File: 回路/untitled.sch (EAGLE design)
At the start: 213 parts, among them Q1 2SJ626, Q2 2SJ626, Q3 BSS138, Q4 BSS138, Q5 2SJ626, Q6 BSS138, Q7 BSS138

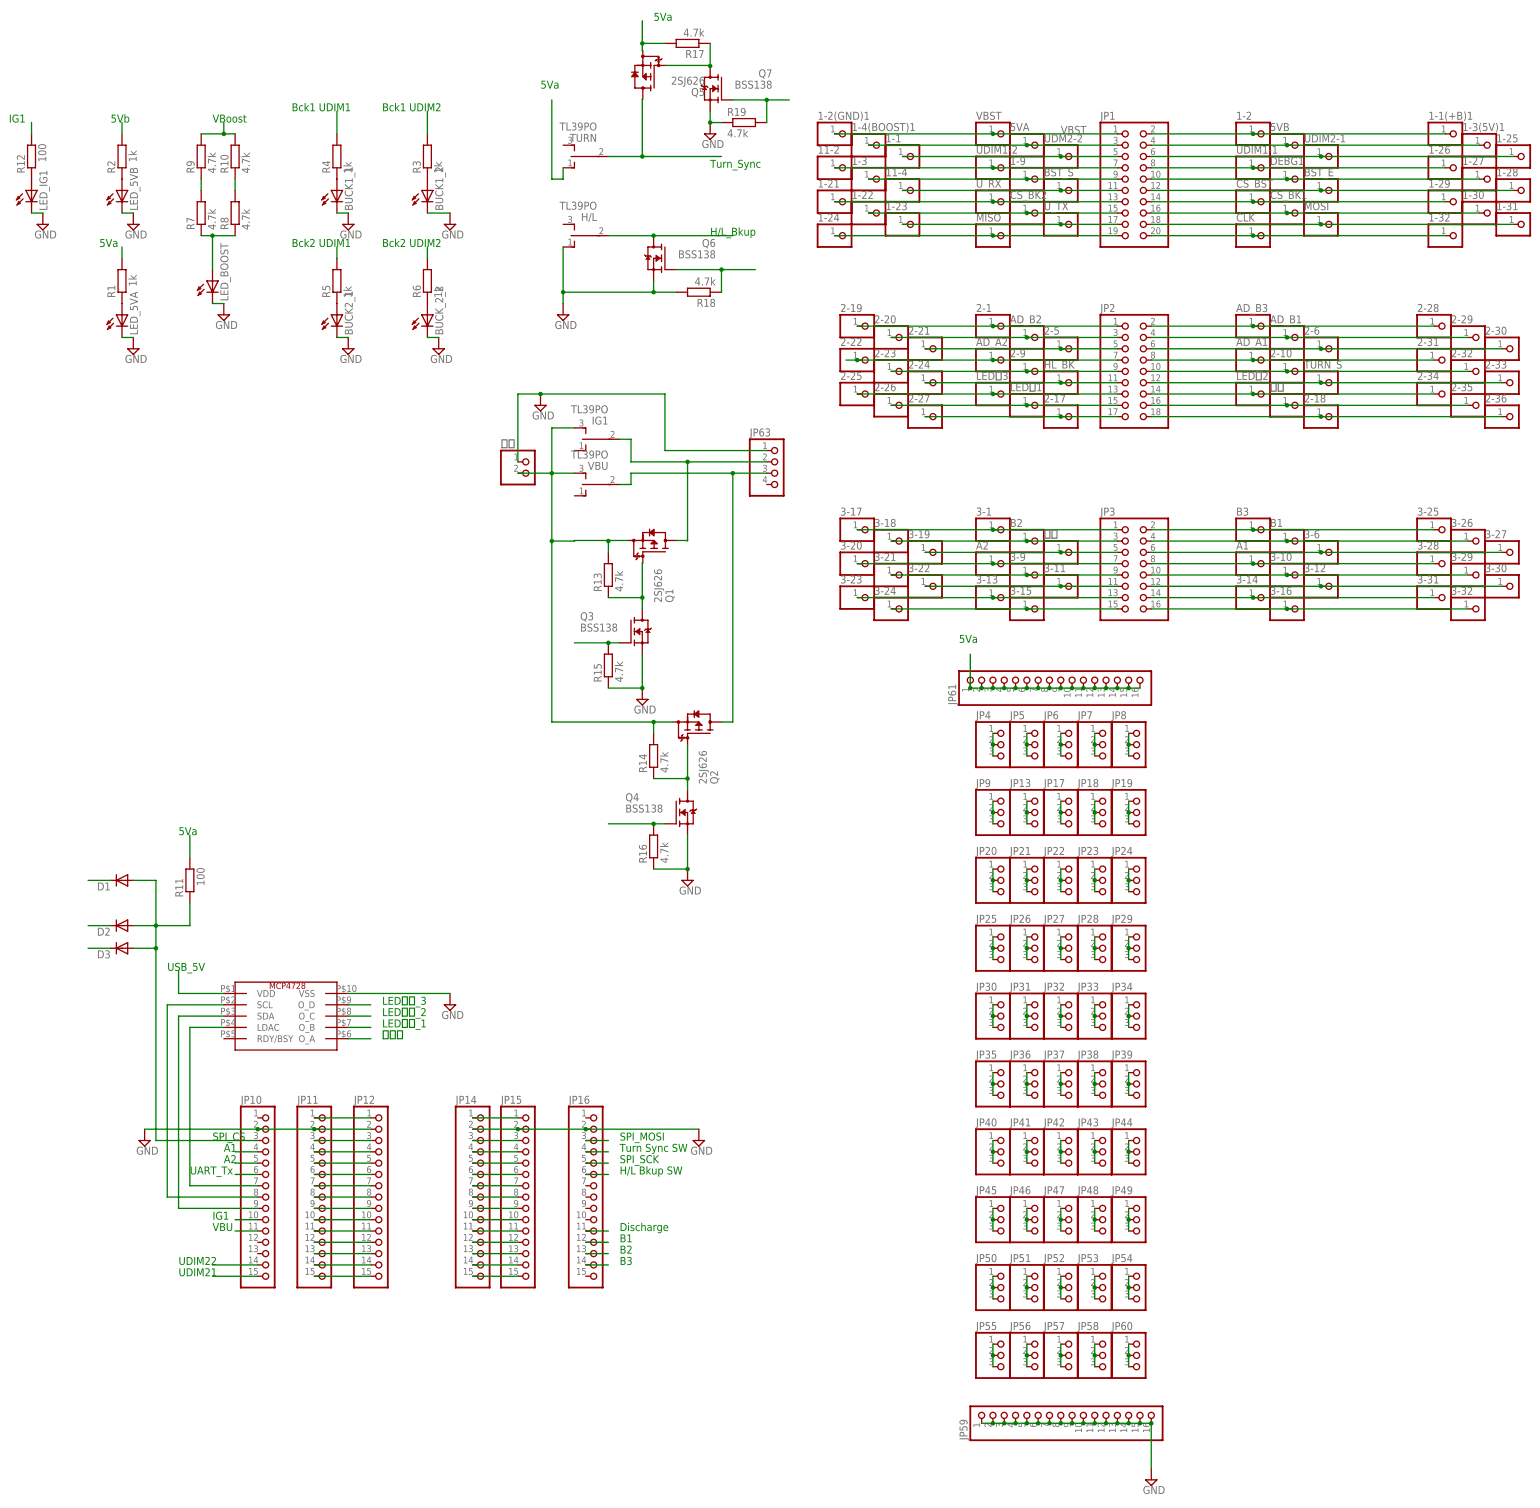
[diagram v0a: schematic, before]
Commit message: 仕様追加 　・LINの読み出し追加 　・Orgログ出力フォーマットの変更
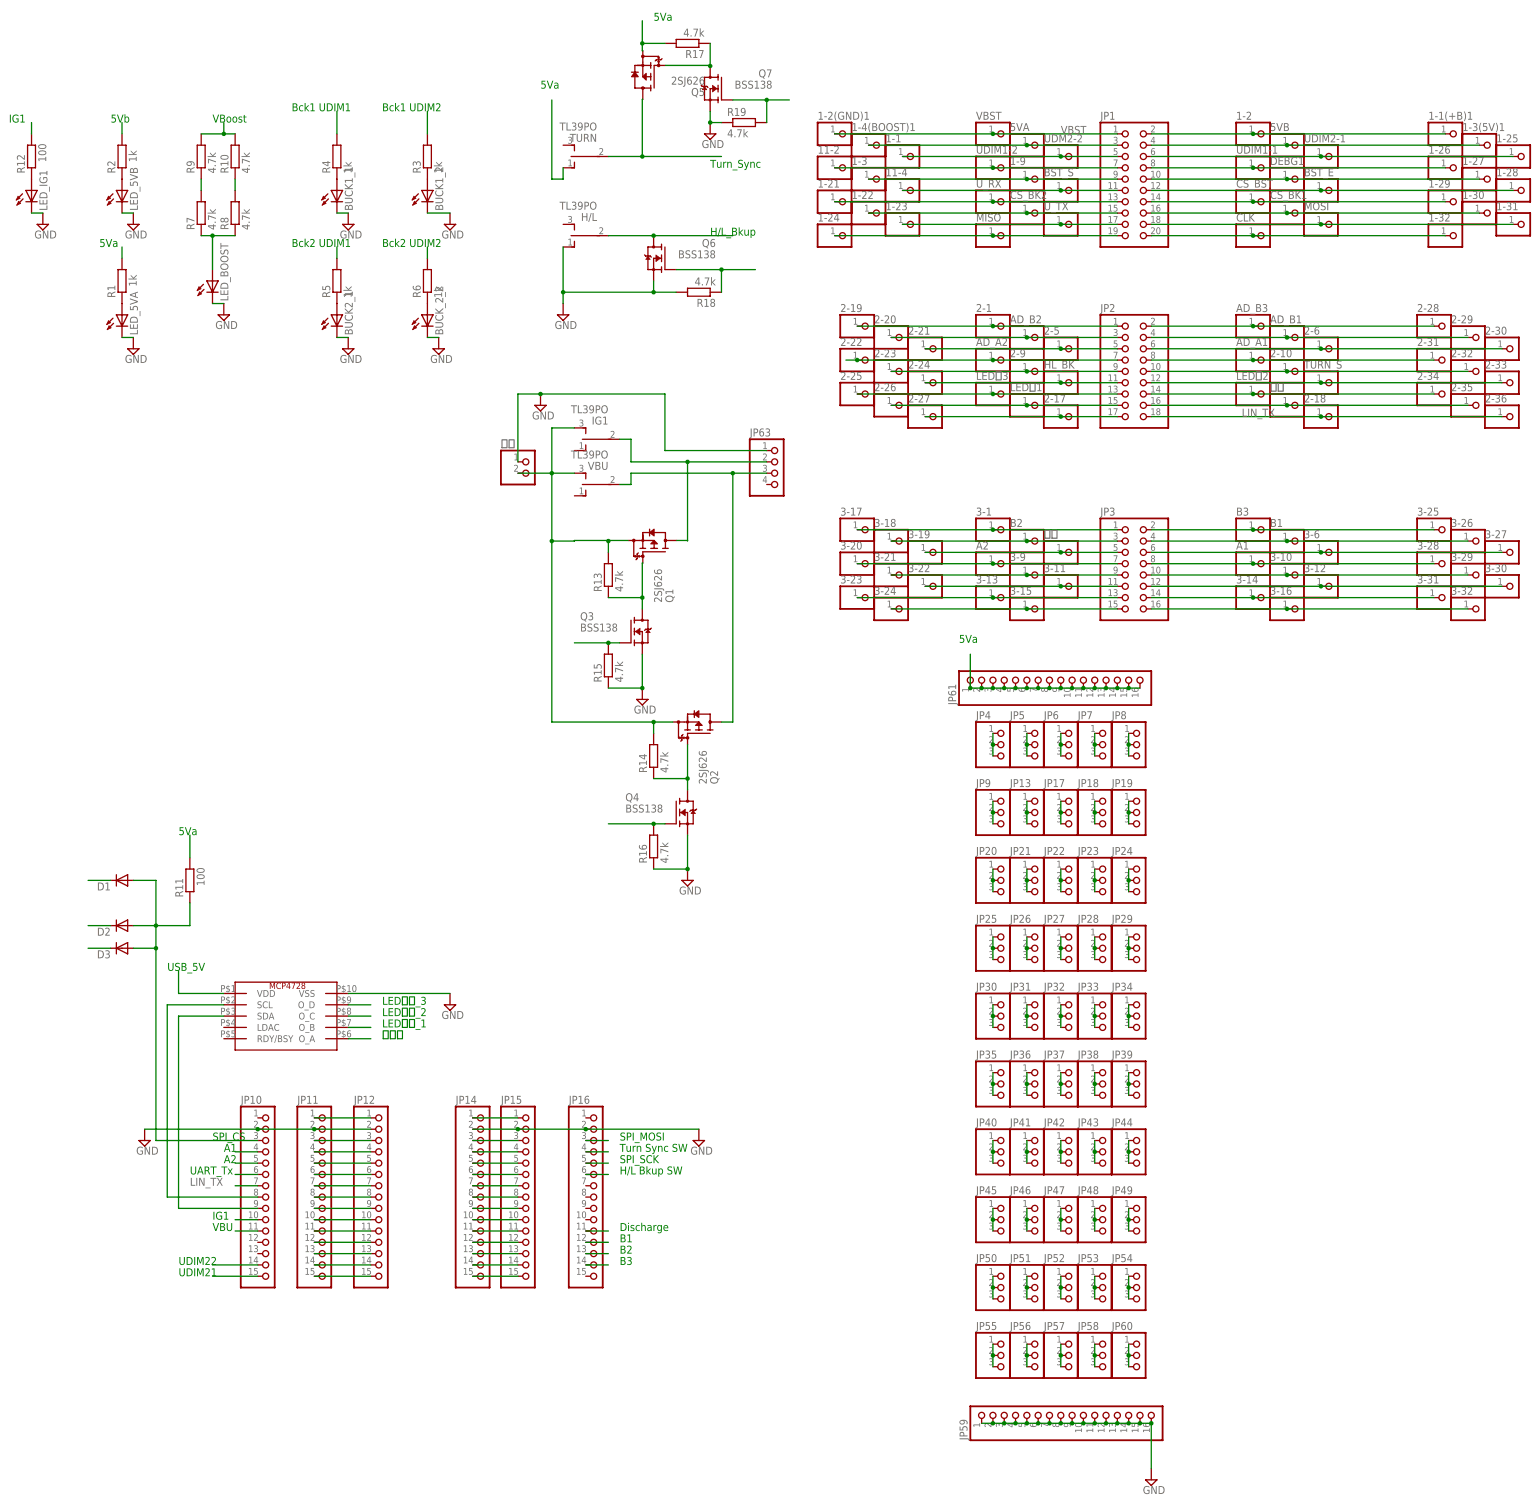
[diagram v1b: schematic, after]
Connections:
- removed net N$30: 2-18.1, 2-36.1, JP2.18
- removed net N$69: JP10.7, U$1.LDAC
- new net LIN_TX: 2-18.1, 2-36.1, JP10.7, JP2.18
